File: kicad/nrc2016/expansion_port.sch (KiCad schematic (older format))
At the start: 2 parts

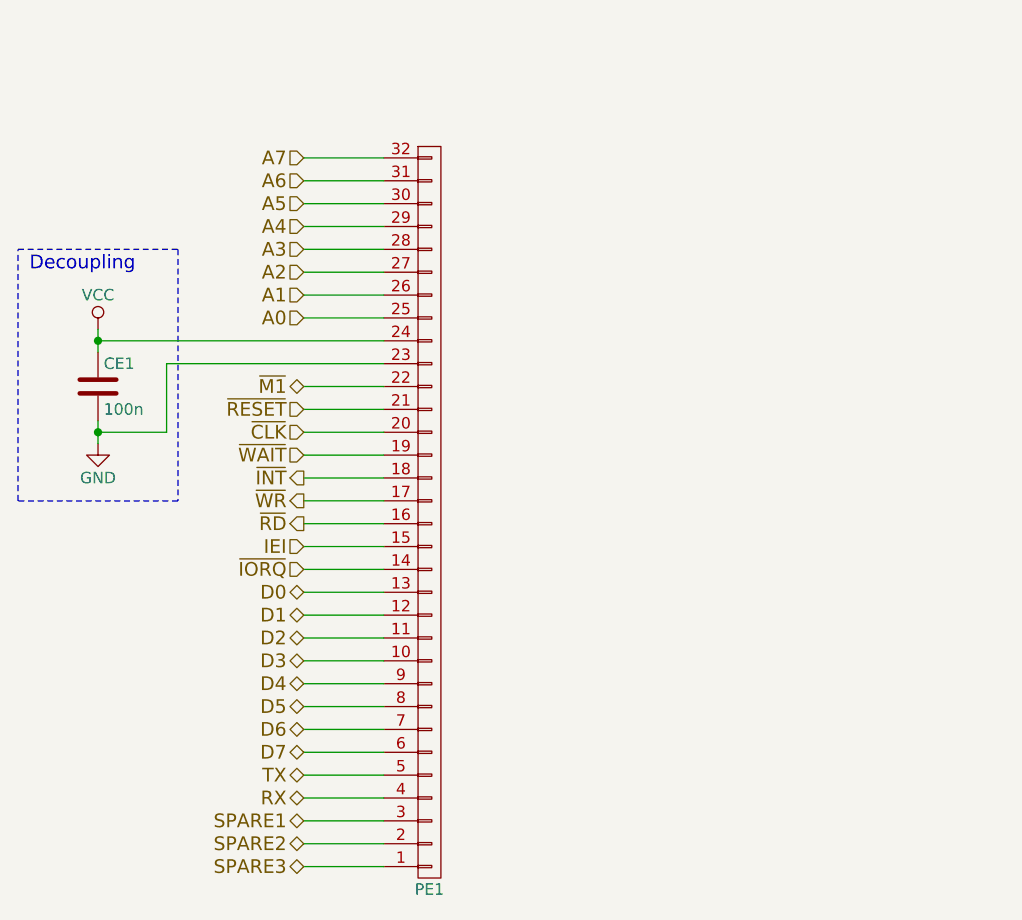
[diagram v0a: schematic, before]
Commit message: Update nrc2016 schema and PCB to use new library symbols
I've added proper schematic symbols for the pre-defined bus sockets to
stop confusion and error by just using the generic "library" socket
component and then relying on the net names to define the pins. Screwed
me once with the VCC and GND switch around, not going to happen again.
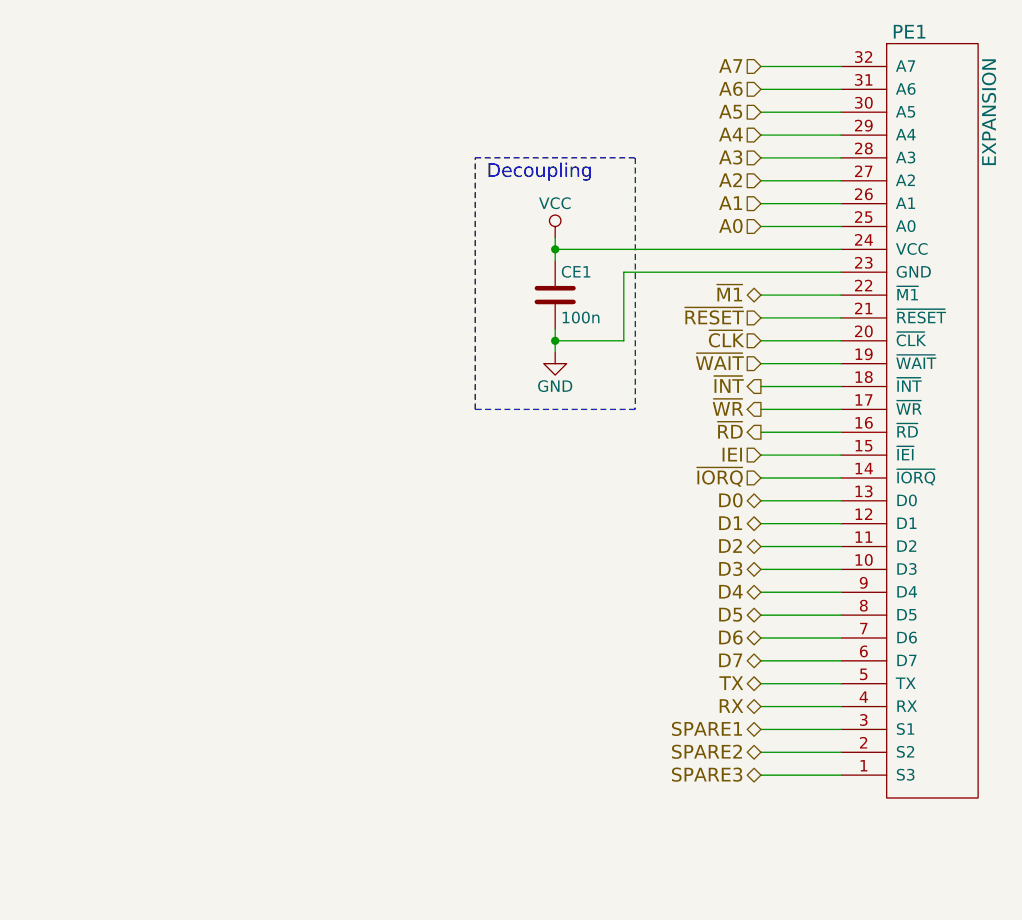
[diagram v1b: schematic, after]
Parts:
- removed PE1: CONN_01X32, Socket_Strips:Socket_Strip_Angled_1x32, symbol CONN_01X32
- added PE1: EXPANSION, Socket_Strips:Socket_Strip_Straight_1x32, symbol EXPANSION
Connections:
- net A0: now also PE1.25 (A0)
- net A1: now also PE1.26 (A1)
- net A2: now also PE1.27 (A2)
- net A3: now also PE1.28 (A3)
- net A4: now also PE1.29 (A4)
- net A5: now also PE1.30 (A5)
- net A6: now also PE1.31 (A6)
- net A7: now also PE1.32 (A7)
- net D0: now also PE1.13 (D0)
- net D1: now also PE1.12 (D1)
- net D2: now also PE1.11 (D2)
- net D3: now also PE1.10 (D3)
- net D4: now also PE1.9 (D4)
- net D5: now also PE1.8 (D5)
- net D6: now also PE1.7 (D6)
- net D7: now also PE1.6 (D7)
- net GND: now also PE1.23 (GND)
- net IEI: now also PE1.15 (~IEI)
- net RX: now also PE1.4 (RX)
- net SPARE1: now also PE1.3 (S1)
- net SPARE2: now also PE1.2 (S2)
- net SPARE3: now also PE1.1 (S3)
- net TX: now also PE1.5 (TX)
- net VCC: now also PE1.24 (VCC)
- net ~CLK: now also PE1.20 (~CLK)
- net ~INT: now also PE1.18 (~INT)
- net ~IORQ: now also PE1.14 (~IORQ)
- net ~M1: now also PE1.22 (~M1)
- net ~RD: now also PE1.16 (~RD)
- net ~RESET: now also PE1.21 (~RESET)
- net ~WAIT: now also PE1.19 (~WAIT)
- net ~WR: now also PE1.17 (~WR)
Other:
- moved on the sheet: CE1
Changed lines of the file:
@@
 LIBS:valves
 LIBS:Zilog
-LIBS:microchip_pic18mcu
-LIBS:6850
 LIBS:nrc2016
 LIBS:atf16v8cv
-LIBS:62256
-LIBS:mcp2221a
 LIBS:z80-cache
 EELAYER 25 0
@@
 Comment4 ""
 $EndDescr
-Text HLabel 3500 3450 0    60   Input ~ 0
+Text HLabel 5500 3050 0    60   Input ~ 0
 A0
-Text HLabel 3500 3350 0    60   Input ~ 0
+Text HLabel 5500 2950 0    60   Input ~ 0
 A1
-Text HLabel 3500 3250 0    60   Input ~ 0
+Text HLabel 5500 2850 0    60   Input ~ 0
 A2
-Text HLabel 3500 3150 0    60   Input ~ 0
+Text HLabel 5500 2750 0    60   Input ~ 0
 A3
-Text HLabel 3500 3050 0    60   Input ~ 0
+Text HLabel 5500 2650 0    60   Input ~ 0
 A4
-Text HLabel 3500 2950 0    60   Input ~ 0
+Text HLabel 5500 2550 0    60   Input ~ 0
 A5
-Text HLabel 3500 2850 0    60   Input ~ 0
+Text HLabel 5500 2450 0    60   Input ~ 0
 A6
-Text HLabel 3500 2750 0    60   Input ~ 0
+Text HLabel 5500 2350 0    60   Input ~ 0
 A7
-Text HLabel 3500 4650 0    60   3State ~ 0
+Text HLabel 5500 4250 0    60   3State ~ 0
 D0
-Text HLabel 3500 4750 0    60   3State ~ 0
+Text HLabel 5500 4350 0    60   3State ~ 0
 D1
-Text HLabel 3500 4850 0    60   3State ~ 0
+Text HLabel 5500 4450 0    60   3State ~ 0
 D2
-Text HLabel 3500 4950 0    60   3State ~ 0
+Text HLabel 5500 4550 0    60   3State ~ 0
 D3
-Text HLabel 3500 5050 0    60   3State ~ 0
+Text HLabel 5500 4650 0    60   3State ~ 0
 D4
-Text HLabel 3500 5150 0    60   3State ~ 0
+Text HLabel 5500 4750 0    60   3State ~ 0
 D5
-Text HLabel 3500 5250 0    60   3State ~ 0
+Text HLabel 5500 4850 0    60   3State ~ 0
 D6
-Text HLabel 3500 5350 0    60   3State ~ 0
+Text HLabel 5500 4950 0    60   3State ~ 0
 D7
-Text HLabel 3500 3750 0    60   3State ~ 0
+Text HLabel 5500 3350 0    60   3State ~ 0
 ~M1
-Text HLabel 3500 4550 0    60   Input ~ 0
+Text HLabel 5500 4150 0    60   Input ~ 0
 ~IORQ
 Wire Wire Line
-	3500 2750 3850 2750
-Wire Wire Line
-	3500 2850 3850 2850
-Wire Wire Line
-	3500 2950 3850 2950
-Wire Wire Line
-	3500 3050 3850 3050
-Wire Wire Line
-	3500 3150 3850 3150
-Wire Wire Line
-	3500 3250 3850 3250
-Wire Wire Line
-	3500 3350 3850 3350
-Wire Wire Line
-	3500 3450 3850 3450
-Wire Wire Line
-	3500 4550 3850 4550
-Wire Wire Line
-	3500 4650 3850 4650
-Wire Wire Line
-	3500 4750 3850 4750
-Wire Wire Line
-	3500 4850 3850 4850
-Wire Wire Line
-	3500 4950 3850 4950
-Wire Wire Line
-	3500 5050 3850 5050
-Wire Wire Line
-	3500 5150 3850 5150
-Wire Wire Line
-	3500 5250 3850 5250
-Wire Wire Line
-	3500 4350 3850 4350
-Wire Wire Line
-	3500 4450 3850 4450
-Wire Wire Line
-	3850 3750 3500 3750
-Wire Wire Line
-	3850 5650 3500 5650
-Wire Wire Line
-	3850 5750 3500 5750
-Wire Wire Line
-	3850 5850 3500 5850
-Text HLabel 3500 5650 0    60   BiDi ~ 0
+	5500 2350 5850 2350
+Wire Wire Line
+	5500 2450 5850 2450
+Wire Wire Line
+	5500 2550 5850 2550
+Wire Wire Line
+	5500 2650 5850 2650
+Wire Wire Line
+	5500 2750 5850 2750
+Wire Wire Line
+	5500 2850 5850 2850
+Wire Wire Line
+	5500 2950 5850 2950
+Wire Wire Line
+	5500 3050 5850 3050
+Wire Wire Line
+	5500 4150 5850 4150
+Wire Wire Line
+	5500 4250 5850 4250
+Wire Wire Line
+	5500 4350 5850 4350
+Wire Wire Line
+	5500 4450 5850 4450
+Wire Wire Line
+	5500 4550 5850 4550
+Wire Wire Line
+	5500 4650 5850 4650
+Wire Wire Line
+	5500 4750 5850 4750
+Wire Wire Line
+	5500 4850 5850 4850
+Wire Wire Line
+	5500 3950 5850 3950
+Wire Wire Line
+	5500 4050 5850 4050
+Wire Wire Line
+	5850 3350 5500 3350
+Wire Wire Line
+	5850 5250 5500 5250
+Wire Wire Line
+	5850 5350 5500 5350
+Wire Wire Line
+	5850 5450 5500 5450
+Text HLabel 5500 5250 0    60   BiDi ~ 0
 SPARE1
-Text HLabel 3500 5750 0    60   BiDi ~ 0
+Text HLabel 5500 5350 0    60   BiDi ~ 0
 SPARE2
-Text HLabel 3500 5850 0    60   BiDi ~ 0
+Text HLabel 5500 5450 0    60   BiDi ~ 0
 SPARE3
 Wire Wire Line
-	3850 3850 3500 3850
-Wire Wire Line
-	3850 3950 3500 3950
-Wire Wire Line
-	3850 4050 3500 4050
-Wire Wire Line
-	3850 4250 3500 4250
-Text HLabel 3500 3850 0    60   Input ~ 0
+	5850 3450 5500 3450
+Wire Wire Line
+	5850 3550 5500 3550
+Wire Wire Line
+	5850 3650 5500 3650
+Wire Wire Line
+	5850 3850 5500 3850
+Text HLabel 5500 3450 0    60   Input ~ 0
 ~RESET
-Text HLabel 3500 3950 0    60   Input ~ 0
+Text HLabel 5500 3550 0    60   Input ~ 0
 ~CLK
-Text HLabel 3500 4150 0    60   Output ~ 0
+Text HLabel 5500 3750 0    60   Output ~ 0
 ~INT
-Text HLabel 3500 4250 0    60   Output ~ 0
+Text HLabel 5500 3850 0    60   Output ~ 0
 ~WR
-Text HLabel 3500 4350 0    60   Output ~ 0
+Text HLabel 5500 3950 0    60   Output ~ 0
 ~RD
-Text HLabel 3500 4450 0    60   Input ~ 0
+Text HLabel 5500 4050 0    60   Input ~ 0
 IEI
 Wire Wire Line
-	2600 3550 3850 3550
-Wire Wire Line
-	2900 3650 3850 3650
+	4600 3150 5850 3150
+Wire Wire Line
+	4900 3250 5850 3250
 $Comp
 L C CE1
 U 1 1 57BF4B26
-P 2600 3750
-F 0 "CE1" H 2625 3850 50  0000 L CNN
-F 1 "100n" H 2625 3650 50  0000 L CNN
-F 2 "Capacitors_ThroughHole:C_Rect_L4_W2.5_P2.5" H 2638 3600 50  0001 C CNN
-F 3 "" H 2600 3750 50  0000 C CNN
-	1    2600 3750
-	1    0    0    -1
-$EndComp
-Wire Wire Line
-	2600 3500 2600 3600
-Wire Wire Line
-	2600 3900 2600 4000
+P 4600 3350
+F 0 "CE1" H 4625 3450 50  0000 L CNN
+F 1 "100n" H 4625 3250 50  0000 L CNN
+F 2 "Capacitors_ThroughHole:C_Rect_L4_W2.5_P2.5" H 4638 3200 50  0001 C CNN
+F 3 "" H 4600 3350 50  0000 C CNN
+	1    4600 3350
+	1    0    0    -1
+$EndComp
+Wire Wire Line
+	4600 3100 4600 3200
+Wire Wire Line
+	4600 3500 4600 3600
 $Comp
 L VCC #PWR033
 U 1 1 57BF4B2F
-P 2600 3500
-F 0 "#PWR033" H 2600 3350 50  0001 C CNN
-F 1 "VCC" H 2600 3650 50  0000 C CNN
-F 2 "" H 2600 3500 50  0000 C CNN
-F 3 "" H 2600 3500 50  0000 C CNN
-	1    2600 3500
+P 4600 3100
+F 0 "#PWR033" H 4600 2950 50  0001 C CNN
+F 1 "VCC" H 4600 3250 50  0000 C CNN
+F 2 "" H 4600 3100 50  0000 C CNN
+F 3 "" H 4600 3100 50  0000 C CNN
+	1    4600 3100
 	1    0    0    -1
 $EndComp
@@
 L GND #PWR034
 U 1 1 57BF4B35
-P 2600 4000
-F 0 "#PWR034" H 2600 3750 50  0001 C CNN
-F 1 "GND" H 2600 3850 50  0000 C CNN
-F 2 "" H 2600 4000 50  0000 C CNN
-F 3 "" H 2600 4000 50  0000 C CNN
-	1    2600 4000
-	1    0    0    -1
-$EndComp
-Text Notes 2300 3250 0    60   ~ 0
+P 4600 3600
+F 0 "#PWR034" H 4600 3350 50  0001 C CNN
+F 1 "GND" H 4600 3450 50  0000 C CNN
+F 2 "" H 4600 3600 50  0000 C CNN
+F 3 "" H 4600 3600 50  0000 C CNN
+	1    4600 3600
+	1    0    0    -1
+$EndComp
+Text Notes 4300 2850 0    60   ~ 0
 Decoupling
 Wire Notes Line
-	2250 3150 2950 3150
-Wire Notes Line
-	2950 3150 2950 4250
-Wire Notes Line
-	2950 4250 2250 4250
-Wire Notes Line
-	2250 4250 2250 3150
-Wire Wire Line
-	2900 3650 2900 3950
-Connection ~ 2600 3550
-Wire Wire Line
-	2900 3950 2600 3950
-Connection ~ 2600 3950
-$Comp
-L CONN_01X32 PE1
-U 1 1 57BF4E4B
-P 4050 4300
-F 0 "PE1" H 4050 5950 50  0000 C CNN
-F 1 "CONN_01X32" V 4150 4300 50  0001 C CNN
-F 2 "Socket_Strips:Socket_Strip_Angled_1x32" H 4050 4300 50  0001 C CNN
-F 3 "" H 4050 4300 50  0000 C CNN
-	1    4050 4300
-	1    0    0    1
-$EndComp
-Wire Wire Line
-	3850 5350 3500 5350
-Wire Wire Line
-	3500 5450 3850 5450
-Text HLabel 3500 5550 0    60   BiDi ~ 0
+	4250 2750 4950 2750
+Wire Notes Line
+	4950 2750 4950 3850
+Wire Notes Line
+	4950 3850 4250 3850
+Wire Notes Line
+	4250 3850 4250 2750
+Wire Wire Line
+	4900 3250 4900 3550
+Connection ~ 4600 3150
+Wire Wire Line
+	4900 3550 4600 3550
+Connection ~ 4600 3550
+Wire Wire Line
+	5850 4950 5500 4950
+Wire Wire Line
+	5500 5050 5850 5050
+Text HLabel 5500 5150 0    60   BiDi ~ 0
 RX
-Text HLabel 3500 5450 0    60   BiDi ~ 0
+Text HLabel 5500 5050 0    60   BiDi ~ 0
 TX
 Wire Wire Line
-	3500 4150 3850 4150
-Text HLabel 3500 4050 0    60   Input ~ 0
+	5500 3750 5850 3750
+Text HLabel 5500 3650 0    60   Input ~ 0
 ~WAIT
 Wire Wire Line
-	3500 5550 3850 5550
+	5500 5150 5850 5150
+$Comp
+L EXPANSION PE1
+U 1 1 57D4785E
+P 6050 2250
+F 0 "PE1" H 6150 2300 60  0000 C CNN
+F 1 "EXPANSION" V 6500 1950 60  0000 C CNN
+F 2 "Socket_Strips:Socket_Strip_Straight_1x32" H 5850 2300 60  0001 C CNN
+F 3 "" H 5850 2300 60  0000 C CNN
+	1    6050 2250
+	1    0    0    -1
+$EndComp
 $EndSCHEMATC

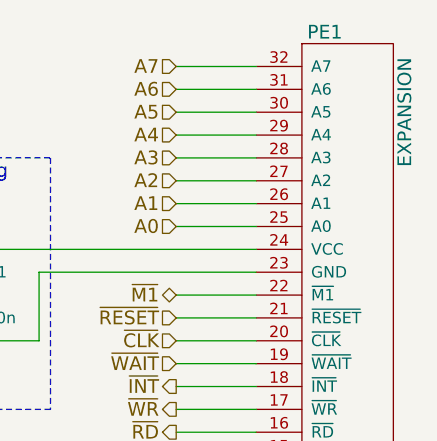
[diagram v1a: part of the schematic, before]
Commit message: More moving things around. Added sockets and pins symbols
Makes it easier for DRC and has hints for the right footprints already.
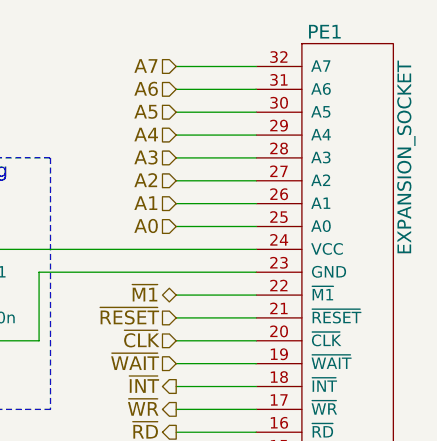
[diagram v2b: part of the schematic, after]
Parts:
- removed PE1: EXPANSION, Socket_Strips:Socket_Strip_Straight_1x32, symbol EXPANSION
- added PE1: EXPANSION_SOCKET, Socket_Strips:Socket_Strip_Angled_1x32, symbol EXPANSION_SOCKET
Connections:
- net A0: now also PE1.25 (A0)
- net A1: now also PE1.26 (A1)
- net A2: now also PE1.27 (A2)
- net A3: now also PE1.28 (A3)
- net A4: now also PE1.29 (A4)
- net A5: now also PE1.30 (A5)
- net A6: now also PE1.31 (A6)
- net A7: now also PE1.32 (A7)
- net D0: now also PE1.13 (D0)
- net D1: now also PE1.12 (D1)
- net D2: now also PE1.11 (D2)
- net D3: now also PE1.10 (D3)
- net D4: now also PE1.9 (D4)
- net D5: now also PE1.8 (D5)
- net D6: now also PE1.7 (D6)
- net D7: now also PE1.6 (D7)
- net GND: now also PE1.23 (GND)
- net IEI: now also PE1.15 (~IEI)
- net RX: now also PE1.4 (RX)
- net SPARE1: now also PE1.3 (S1)
- net SPARE2: now also PE1.2 (S2)
- net SPARE3: now also PE1.1 (S3)
- net TX: now also PE1.5 (TX)
- net VCC: now also PE1.24 (VCC)
- net ~CLK: now also PE1.20 (~CLK)
- net ~INT: now also PE1.18 (~INT)
- net ~IORQ: now also PE1.14 (~IORQ)
- net ~M1: now also PE1.22 (~M1)
- net ~RD: now also PE1.16 (~RD)
- net ~RESET: now also PE1.21 (~RESET)
- net ~WAIT: now also PE1.19 (~WAIT)
- net ~WR: now also PE1.17 (~WR)
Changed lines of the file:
@@
 	5500 5150 5850 5150
 $Comp
-L EXPANSION PE1
-U 1 1 57D4785E
+L EXPANSION_SOCKET PE1
+U 1 1 57D437B9
 P 6050 2250
 F 0 "PE1" H 6150 2300 60  0000 C CNN
-F 1 "EXPANSION" V 6500 1950 60  0000 C CNN
-F 2 "Socket_Strips:Socket_Strip_Straight_1x32" H 5850 2300 60  0001 C CNN
+F 1 "EXPANSION_SOCKET" V 6500 1750 60  0000 C CNN
+F 2 "Socket_Strips:Socket_Strip_Angled_1x32" H 5850 2300 60  0001 C CNN
 F 3 "" H 5850 2300 60  0000 C CNN
 	1    6050 2250
